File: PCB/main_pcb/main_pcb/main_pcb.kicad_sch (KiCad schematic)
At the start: 50 parts, among them J1 Conn_01x20_Socket, J2 Conn_01x20_Socket, SW0_Header1 B6B-XH-A, SW1_Header1 B6B-XH-A

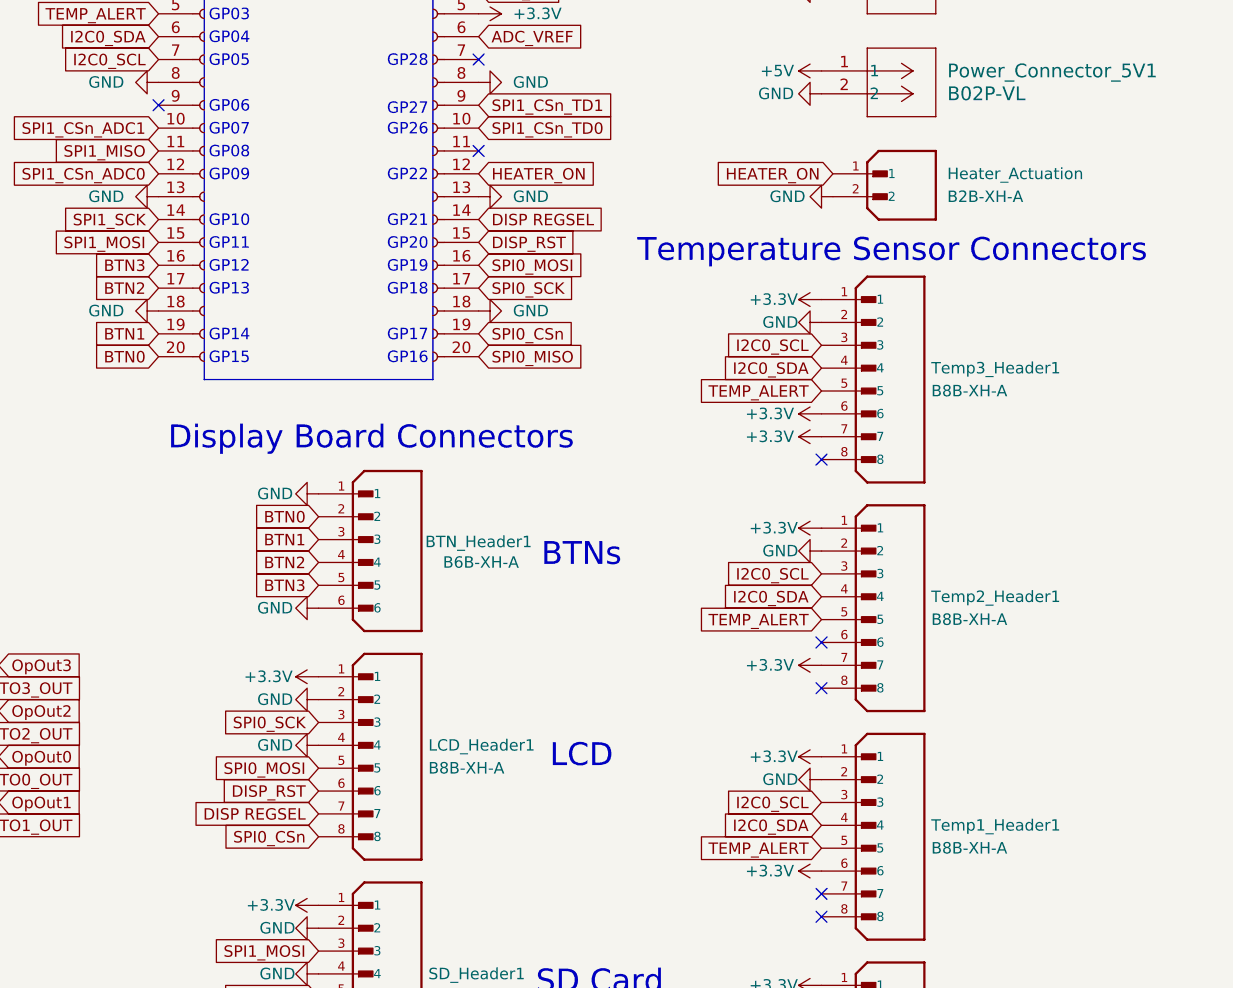
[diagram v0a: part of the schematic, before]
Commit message: Updated and tweaked main PCB
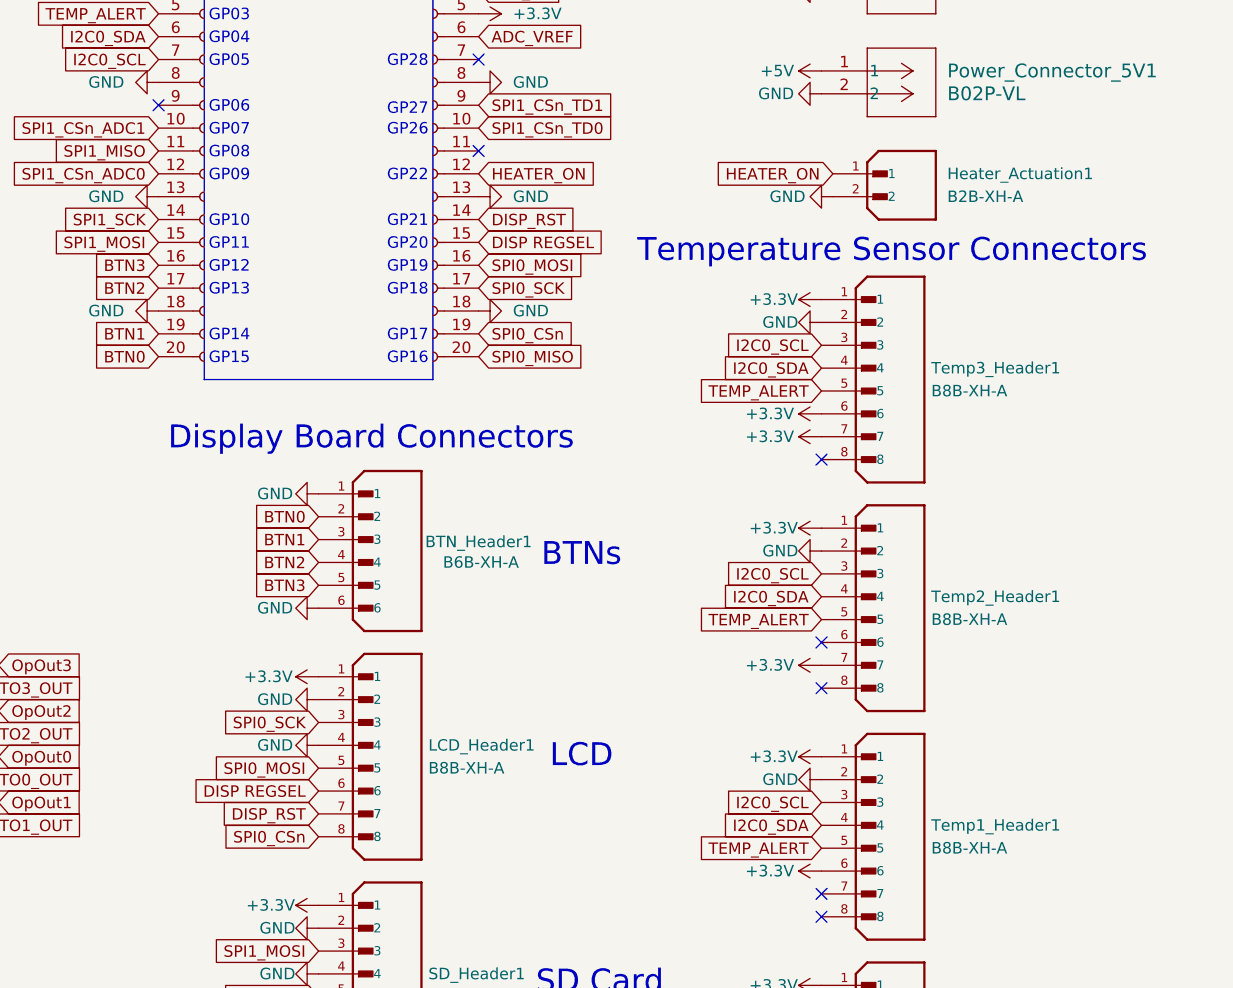
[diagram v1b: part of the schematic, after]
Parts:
- C0, C1, C2, C3, C4, C5, C6, C7, C8, C9: footprint C1206C101K1HACTU:CAPC340180_88N_KEM -> Capacitor_SMD:C_1206_3216Metric_Pad1.33x1.80mm_HandSolder
- Photo0, Photo1, Photo2, Photo3, Photo4, Photo5, Photo7, Photo8, Photo9, UPhoto6: footprint APDS_9006_020:photodiode_v3 -> APDS_9006_020:photodiode_v4
- renumbered Heater_Actuation to Heater_Actuation1
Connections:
- net DISP REGSEL: now also J2.15 (Pin_15), LCD_Header1.6; no longer J2.14 (Pin_14), LCD_Header1.7
- net DISP_RST: now also J2.14 (Pin_14), LCD_Header1.7; no longer J2.15 (Pin_15), LCD_Header1.6
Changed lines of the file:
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@@
 		)
 	)
+	(global_label "DISP REGSEL"
+		(shape input)
+		(at 330.2 54.61 0)
+		(fields_autoplaced yes)
+		(effects
+			(font
+				(size 1.27 1.27)
+			)
+			(justify left)
+		)
+		(property "Intersheetrefs" "${INTERSHEET_REFS}"
+			(at 345.5827 54.61 0)
+			(effects
+				(font
+					(size 1.27 1.27)
+				)
+				(justify left)
+				(hide yes)
+			)
+		)
+	)
 	(global_label "BTN1"
 		(shape input)
@@
 		)
 	)
-	(global_label "DISP_RST"
-		(shape input)
-		(at 330.2 54.61 0)
-		(fields_autoplaced yes)
-		(effects
-			(font
-				(size 1.27 1.27)
-			)
-			(justify left)
-		)
-		(property "Intersheetrefs" "${INTERSHEET_REFS}"
-			(at 341.9542 54.61 0)
-			(effects
-				(font
-					(size 1.27 1.27)
-				)
-				(justify left)
-				(hide yes)
-			)
-		)
-	)
 	(global_label "PHOTO9_OUT"
 		(shape input)
@@
 		)
 	)
-	(global_label "DISP REGSEL"
-		(shape input)
-		(at 330.2 52.07 0)
-		(fields_autoplaced yes)
-		(effects
-			(font
-				(size 1.27 1.27)
-			)
-			(justify left)
-		)
-		(property "Intersheetrefs" "${INTERSHEET_REFS}"
-			(at 345.5827 52.07 0)
-			(effects
-				(font
-					(size 1.27 1.27)
-				)
-				(justify left)
-				(hide yes)
-			)
-		)
-	)
 	(global_label "OpOut3"
 		(shape input)
@@
 	(global_label "DISP_RST"
 		(shape input)
-		(at 312.42 115.57 180)
+		(at 330.2 52.07 0)
 		(fields_autoplaced yes)
 		(effects
@@
 				(size 1.27 1.27)
 			)
-			(justify right)
+			(justify left)
 		)
 		(property "Intersheetrefs" "${INTERSHEET_REFS}"
-			(at 300.6658 115.57 0)
+			(at 341.9542 52.07 0)
 			(effects
 				(font
 					(size 1.27 1.27)
 				)
-				(justify right)
+				(justify left)
 				(hide yes)
 			)
@@
 		)
 	)
+	(global_label "DISP REGSEL"
+		(shape input)
+		(at 312.42 115.57 180)
+		(fields_autoplaced yes)
+		(effects
+			(font
+				(size 1.27 1.27)
+			)
+			(justify right)
+		)
+		(property "Intersheetrefs" "${INTERSHEET_REFS}"
+			(at 297.0373 115.57 0)
+			(effects
+				(font
+					(size 1.27 1.27)
+				)
+				(justify right)
+				(hide yes)
+			)
+		)
+	)
 	(global_label "SPI1_MOSI"
 		(shape input)
@@
 		)
 	)
+	(global_label "DISP_RST"
+		(shape input)
+		(at 312.42 118.11 180)
+		(fields_autoplaced yes)
+		(effects
+			(font
+				(size 1.27 1.27)
+			)
+			(justify right)
+		)
+		(property "Intersheetrefs" "${INTERSHEET_REFS}"
+			(at 300.6658 118.11 0)
+			(effects
+				(font
+					(size 1.27 1.27)
+				)
+				(justify right)
+				(hide yes)
+			)
+		)
+	)
 	(global_label "SPI0_CSn"
 		(shape input)
@@
 		)
 	)
-	(global_label "DISP REGSEL"
-		(shape input)
-		(at 312.42 118.11 180)
-		(fields_autoplaced yes)
-		(effects
-			(font
-				(size 1.27 1.27)
-			)
-			(justify right)
-		)
-		(property "Intersheetrefs" "${INTERSHEET_REFS}"
-			(at 297.0373 118.11 0)
-			(effects
-				(font
-					(size 1.27 1.27)
-				)
-				(justify right)
-				(hide yes)
-			)
-		)
-	)
 	(global_label "SPI1_SCK"
 		(shape input)
@@
 			)
 		)
-		(property "Footprint" "C1206C101K1HACTU:CAPC340180_88N_KEM"
+		(property "Footprint" "Capacitor_SMD:C_1206_3216Metric_Pad1.33x1.80mm_HandSolder"
 			(at 187.96 162.56 0)
 			(effects
@@
 			)
 		)
-		(property "Footprint" "APDS_9006_020:photodiode_v3"
+		(property "Footprint" "APDS_9006_020:photodiode_v4"
 			(at 160.02 132.08 0)
 			(effects
@@
 			)
 		)
-		(property "Footprint" "APDS_9006_020:photodiode_v3"
+		(property "Footprint" "APDS_9006_020:photodiode_v4"
 			(at 160.02 157.48 0)
 			(effects
@@
 		(dnp no)
 		(fields_autoplaced yes)
-		(property "Reference" "Heater_Actuation"
+		(property "Reference" "Heater_Actuation1"
 			(at 382.27 46.9899 0)
 			(effects
@@
 			(project ""
 				(path "/9e1b86fa-37cc-48d2-968d-4a7578d4873f"
-					(reference "Heater_Actuation")
+					(reference "Heater_Actuation1")
 					(unit 1)
 				)
@@
 			)
 		)
-		(property "Footprint" "APDS_9006_020:photodiode_v3"
+		(property "Footprint" "APDS_9006_020:photodiode_v4"
 			(at 96.52 132.08 0)
 			(effects
@@
 			)
 		)
-		(property "Footprint" "C1206C101K1HACTU:CAPC340180_88N_KEM"
+		(property "Footprint" "Capacitor_SMD:C_1206_3216Metric_Pad1.33x1.80mm_HandSolder"
 			(at 187.96 213.36 0)
 			(effects
@@
 			)
 		)
-		(property "Footprint" "APDS_9006_020:photodiode_v3"
+		(property "Footprint" "APDS_9006_020:photodiode_v4"
 			(at 160.02 106.68 0)
 			(effects
@@
 			)
 		)
-		(property "Footprint" "APDS_9006_020:photodiode_v3"
+		(property "Footprint" "APDS_9006_020:photodiode_v4"
 			(at 96.52 157.48 0)
 			(effects
@@
 			)
 		)
-		(property "Footprint" "C1206C101K1HACTU:CAPC340180_88N_KEM"
+		(property "Footprint" "Capacitor_SMD:C_1206_3216Metric_Pad1.33x1.80mm_HandSolder"
 			(at 187.96 111.76 0)
 			(effects
@@
 			)
 		)
-		(property "Footprint" "APDS_9006_020:photodiode_v3"
+		(property "Footprint" "APDS_9006_020:photodiode_v4"
 			(at 160.02 208.28 0)
 			(effects
@@
 			)
 		)
-		(property "Footprint" "C1206C101K1HACTU:CAPC340180_88N_KEM"
+		(property "Footprint" "Capacitor_SMD:C_1206_3216Metric_Pad1.33x1.80mm_HandSolder"
 			(at 124.46 187.96 0)
 			(effects
@@
 			)
 		)
-		(property "Footprint" "C1206C101K1HACTU:CAPC340180_88N_KEM"
+		(property "Footprint" "Capacitor_SMD:C_1206_3216Metric_Pad1.33x1.80mm_HandSolder"
 			(at 124.46 162.56 0)
 			(effects
@@
 			)
 		)
-		(property "Footprint" "C1206C101K1HACTU:CAPC340180_88N_KEM"
+		(property "Footprint" "Capacitor_SMD:C_1206_3216Metric_Pad1.33x1.80mm_HandSolder"
 			(at 187.96 187.96 0)
 			(effects
@@
 			)
 		)
-		(property "Footprint" "APDS_9006_020:photodiode_v3"
+		(property "Footprint" "APDS_9006_020:photodiode_v4"
 			(at 96.52 208.28 0)
 			(effects
@@
 			)
 		)
-		(property "Footprint" "C1206C101K1HACTU:CAPC340180_88N_KEM"
+		(property "Footprint" "Capacitor_SMD:C_1206_3216Metric_Pad1.33x1.80mm_HandSolder"
 			(at 124.46 111.76 0)
 			(effects
@@
 			)
 		)
-		(property "Footprint" "C1206C101K1HACTU:CAPC340180_88N_KEM"
+		(property "Footprint" "Capacitor_SMD:C_1206_3216Metric_Pad1.33x1.80mm_HandSolder"
 			(at 187.96 137.16 0)
 			(effects
@@
 			)
 		)
-		(property "Footprint" "APDS_9006_020:photodiode_v3"
+		(property "Footprint" "APDS_9006_020:photodiode_v4"
 			(at 96.52 106.68 0)
 			(effects
@@
 			)
 		)
-		(property "Footprint" "C1206C101K1HACTU:CAPC340180_88N_KEM"
+		(property "Footprint" "Capacitor_SMD:C_1206_3216Metric_Pad1.33x1.80mm_HandSolder"
 			(at 124.46 137.16 0)
 			(effects
@@
 			)
 		)
-		(property "Footprint" "APDS_9006_020:photodiode_v3"
+		(property "Footprint" "APDS_9006_020:photodiode_v4"
 			(at 96.52 182.88 0)
 			(effects
@@
 			)
 		)
-		(property "Footprint" "APDS_9006_020:photodiode_v3"
+		(property "Footprint" "APDS_9006_020:photodiode_v4"
 			(at 160.02 182.88 0)
 			(effects
@@
 			)
 		)
-		(property "Footprint" "C1206C101K1HACTU:CAPC340180_88N_KEM"
+		(property "Footprint" "Capacitor_SMD:C_1206_3216Metric_Pad1.33x1.80mm_HandSolder"
 			(at 124.46 213.36 0)
 			(effects

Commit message: Fixed some stuff and made the main PCB smaller.
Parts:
- removed Fan_Header1: B8B-XH-A, Connector_JST:JST_XH_B8B-XH-A_1x08_P2.50mm_Vertical, symbol B8B-XH-A:B8B-XH-A
- added Fan_Header1: B2B-XH-A, B2B_XH_A:JST_B2B-XH-A, symbol B2B-XH-A:B2B-XH-A
- added J3: Conn_01x09_Socket, Connector_PinSocket_2.54mm:PinSocket_1x09_P2.54mm_Vertical, symbol Connector:Conn_01x09_Socket
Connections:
- net VSYS is gone; now on net +3.3V: J2.2 (Pin_2)
- net +3.3V: no longer J2.5 (Pin_5)
- net +5V: now also Fan_Header1.2
- net 3V3_EN: now also J3.4 (Pin_4)
- net ADC_VREF: now also J3.6 (Pin_6)
- net GND: now also Fan_Header1.1
- net VBUS: now also J3.3 (Pin_3)
- net RUN: now reaches J2.11 (Pin_11)
- net RUN: now also J3.8 (Pin_8)
- net GPIO29: now reaches J2.7 (Pin_7)
- net GPIO29: now also J3.7 (Pin_7)
- net GPIO1: now reaches J1.2 (Pin_2)
- net GPIO1: now also J3.1 (Pin_1)
- net GPIO2: now reaches J1.4 (Pin_4)
- net GPIO2: now also J3.2 (Pin_2)
- net GPIO6: now reaches J1.9 (Pin_9)
- net SPI0_MISO renamed GPIO16
- net GPIO16: now also J3.9 (Pin_9)
- new net 3V3_OUT: J2.5 (Pin_5), J3.5 (Pin_5)
- no-connect marks 27 -> 18
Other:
- note added: "VSYS"
